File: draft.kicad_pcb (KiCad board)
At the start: 2 copper layers, 40.6 x 128.5 mm, 35 parts

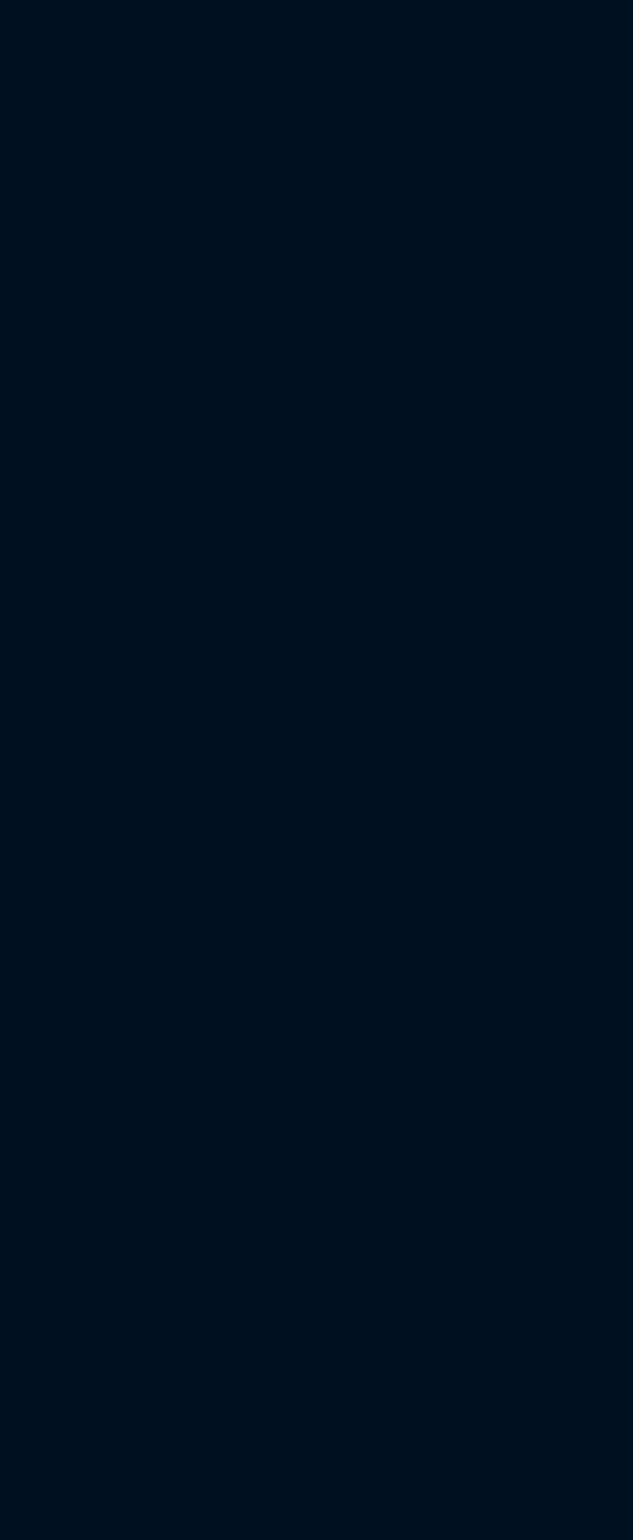
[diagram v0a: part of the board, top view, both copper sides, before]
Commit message: Artworks on pcbs are done.
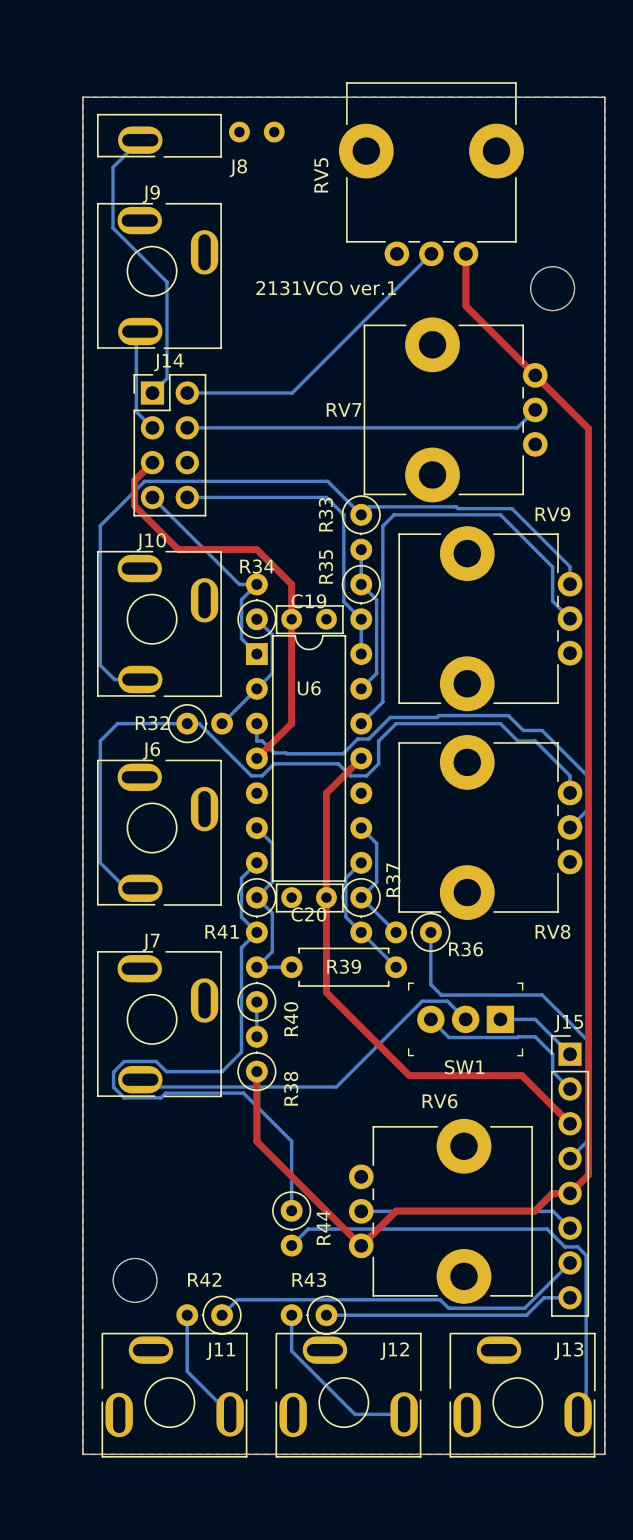
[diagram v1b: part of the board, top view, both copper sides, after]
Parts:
- added C19: 0.1u, Attenuverter:C_Axial_L4.8mm_D2.0mm_P2.54mm_Horizontal, F.Cu at (128.3, 94.0)
- added C20: 0.1u, Attenuverter:C_Axial_L4.8mm_D2.0mm_P2.54mm_Horizontal, F.Cu at (128.3, 114.3)
- added J10: exp FM, Attenuverter:MJ-355_3.5mm_mono_jack, F.Cu at (115.6, 94.0)
- added J11: tri_out, Attenuverter:MJ-355_3.5mm_mono_jack, F.Cu at (116.8, 151.1)
- added J12: saw_out, Attenuverter:MJ-355_3.5mm_mono_jack, F.Cu at (129.5, 151.1)
- added J13: squ_out, Attenuverter:MJ-355_3.5mm_mono_jack, F.Cu at (142.2, 151.1)
- added J14: bus_L, Connector_PinHeader_2.54mm:PinHeader_2x04_P2.54mm_Vertical, F.Cu at (115.6, 77.5)
- added J15: bus_R, Connector_PinHeader_2.54mm:PinHeader_1x08_P2.54mm_Vertical, F.Cu at (146.1, 125.7)
- added J6: lin FM, Attenuverter:MJ-355_3.5mm_mono_jack, F.Cu at (115.6, 109.2)
- added J7: sync, Attenuverter:MJ-355_3.5mm_mono_jack, F.Cu at (115.6, 123.2)
- added J8: V/oct_1, Attenuverter:MJ-355_3.5mm_mono_jack_terminal_only, F.Cu at (115.6, 54.6)
- added J9: V/oct_2, Attenuverter:MJ-355_3.5mm_mono_jack, F.Cu at (115.6, 68.6)
- added R32: 100k, Resistor_THT:R_Axial_DIN0207_L6.3mm_D2.5mm_P2.54mm_Vertical, F.Cu at (118.1, 101.6)
- added R33: 100k, Resistor_THT:R_Axial_DIN0207_L6.3mm_D2.5mm_P2.54mm_Vertical, F.Cu at (130.8, 86.4)
- added R34: 100k, Resistor_THT:R_Axial_DIN0207_L6.3mm_D2.5mm_P2.54mm_Vertical, F.Cu at (123.2, 94.0)
- added R35: 100k, Resistor_THT:R_Axial_DIN0207_L6.3mm_D2.5mm_P2.54mm_Vertical, F.Cu at (130.8, 91.4)
- added R36: 10k, Resistor_THT:R_Axial_DIN0207_L6.3mm_D2.5mm_P2.54mm_Vertical, F.Cu at (135.9, 116.8)
- added R37: 10k, Resistor_THT:R_Axial_DIN0207_L6.3mm_D2.5mm_P2.54mm_Vertical, F.Cu at (130.8, 114.3)
- added R38: 3k, Resistor_THT:R_Axial_DIN0207_L6.3mm_D2.5mm_P2.54mm_Vertical, F.Cu at (123.2, 127.0)
- added R39: 3k, Resistor_THT:R_Axial_DIN0207_L6.3mm_D2.5mm_P7.62mm_Horizontal, F.Cu at (133.3, 119.4)
- added R40: 3k, Resistor_THT:R_Axial_DIN0207_L6.3mm_D2.5mm_P2.54mm_Vertical, F.Cu at (123.2, 121.9)
- added R41: 12k, Resistor_THT:R_Axial_DIN0207_L6.3mm_D2.5mm_P2.54mm_Vertical, F.Cu at (123.2, 114.3)
- added R42: 1k, Resistor_THT:R_Axial_DIN0207_L6.3mm_D2.5mm_P2.54mm_Vertical, F.Cu at (120.7, 144.8)
- added R43: 1k, Resistor_THT:R_Axial_DIN0207_L6.3mm_D2.5mm_P2.54mm_Vertical, F.Cu at (128.3, 144.8)
- added R44: 1k, Resistor_THT:R_Axial_DIN0207_L6.3mm_D2.5mm_P2.54mm_Vertical, F.Cu at (125.7, 137.2)
- added REF**: MountingHole_3.2mm_M3, MountingHole:MountingHole_3.2mm_M3, F.Cu at (114.3, 142.2)
- added REF**: MountingHole_3.2mm_M3, MountingHole:MountingHole_3.2mm_M3, F.Cu at (144.8, 69.8)
- added RV5: 10k, Attenuverter:Potentiometer_Alps_RK09L_Single_Vertical, F.Cu at (138.4, 67.3)
- added RV6: 10k, Attenuverter:Potentiometer_Alps_RK09L_Single_Vertical, F.Cu at (130.8, 139.7)
- added RV7: 10k, Attenuverter:Potentiometer_Alps_RK09L_Single_Vertical, F.Cu at (143.5, 76.2)
- added RV8: 10k, Attenuverter:Potentiometer_Alps_RK09L_Single_Vertical, F.Cu at (146.1, 106.7)
- added RV9: 10k, Attenuverter:Potentiometer_Alps_RK09L_Single_Vertical, F.Cu at (146.1, 91.4)
- added SW1: sync, Attenuverter:Switch_Toggle_on-off-on_akizuki, F.Cu at (138.4, 123.2)
- added U6: TL074, Package_DIP:DIP-14_W7.62mm, F.Cu at (123.2, 96.5)
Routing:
- net /module_interface/Vref: track 0.00 -> 105.5 mm
- net Net-(J6-PadT): track 0.00 -> 55.1 mm
- net Net-(J10-PadT): track 0.00 -> 53.5 mm
- net Net-(R41-Pad2): track 0.00 -> 46.9 mm
- net -12V: track 0.00 -> 39.9 mm
- net Net-(J13-PadT): track 0.00 -> 34.6 mm
- net Net-(RV9-Pad2): track 0.00 -> 33.7 mm
- net Net-(RV8-Pad2): track 0.00 -> 33.1 mm
- net +12V: track 0.00 -> 31.3 mm
- net /module_interface/tri_out: track 0.00 -> 27.5 mm
- net Net-(J7-PadT): track 0.00 -> 27.1 mm
- net /module_interface/squ: track 0.00 -> 26.1 mm
- net /module_interface/fine: track 0.00 -> 25.9 mm
- net /module_interface/exp_fm: track 0.00 -> 22.6 mm
- net /module_interface/freq: track 0.00 -> 22.0 mm
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- added copper zone on B.Cu, net GND
- added copper zone on F.Cu, net GND
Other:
- board size 40.6 x 128.5 mm -> 85.1 x 128.5 mm
- board text added: "2131VCO ver.1"

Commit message: Fixed a minor problem; - position of HF_track and init_freq trimmers - marking in the front panel
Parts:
- + (x2): renamed from -    +
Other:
- board text added: "-"
